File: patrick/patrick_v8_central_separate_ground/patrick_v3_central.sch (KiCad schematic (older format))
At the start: 32 parts, among them J1 Conn_02x05_Counter_Clockwise, J10 61300311121, J2 Conn_02x05_Counter_Clockwise, J3 Conn_02x05_Counter_Clockwise, J4 Conn_02x05_Counter_Clockwise, J5 Conn_02x05_Counter_Clockwise, J6 DM3CS-SF, J7 61300211121, J8 Conn_01x03, Q1 RUE002N02TL, Q2 RUE002N02TL, Q3 RUE002N02TL, U1 ICM-20948, U2 MCP1702T-1802E_CB, U3 BL652-SA-01, U4 PCA9685PW_Q900,118, U5 PCA9685PW_Q900,118, U6 MPM3610GQV-Z

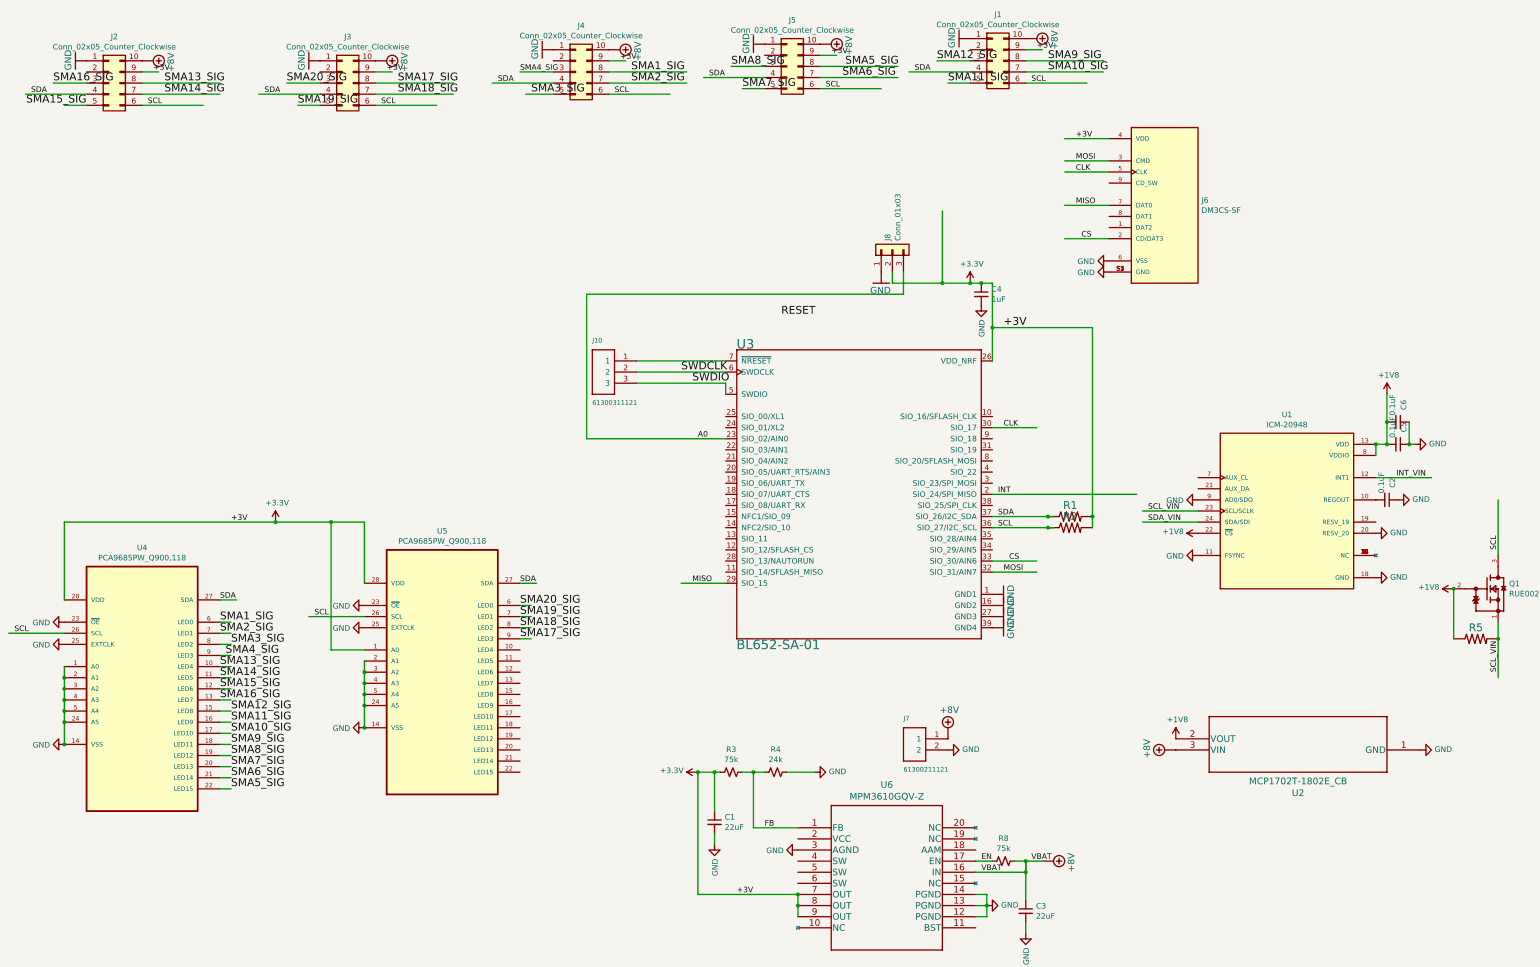
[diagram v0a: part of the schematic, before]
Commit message: separate gnd
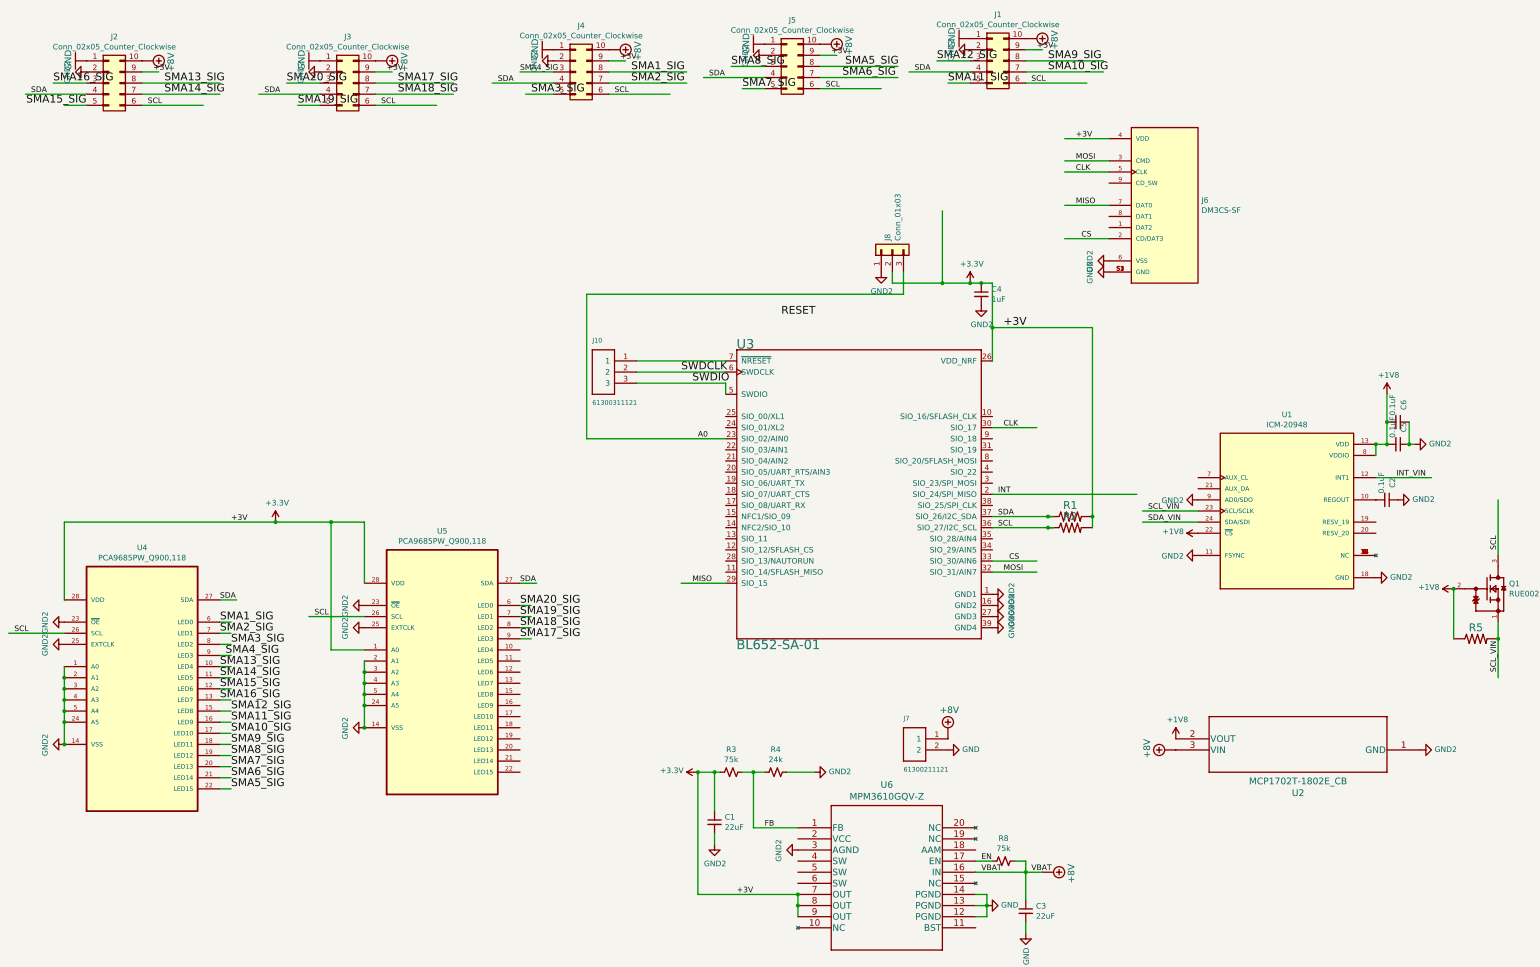
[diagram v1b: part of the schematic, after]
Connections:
- net labels added: GND2
- wire segments 157 -> 156

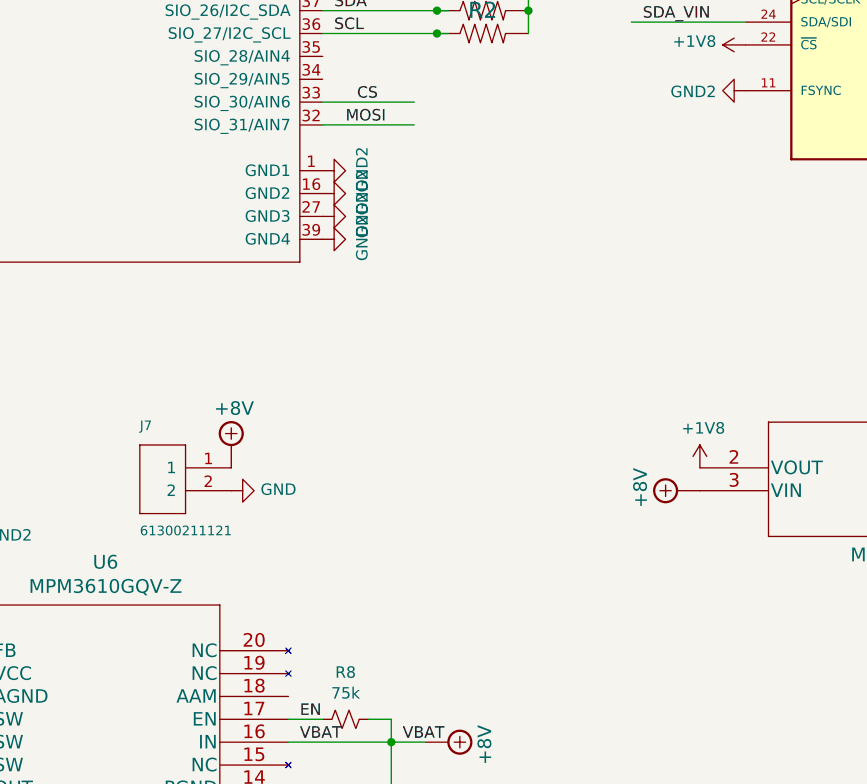
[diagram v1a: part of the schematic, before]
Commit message: separate gnd
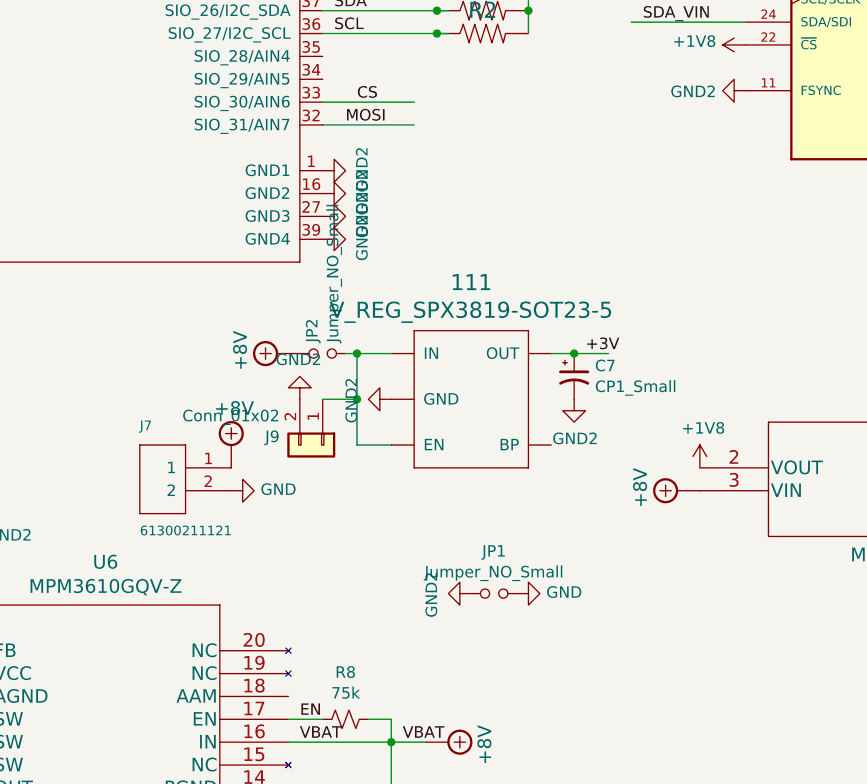
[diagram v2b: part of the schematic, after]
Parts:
- added 111: V_REG_SPX3819-SOT23-5, Package_TO_SOT_SMD:SOT-23-5, symbol patrick_0.5-eagle-import:V_REG_SPX3819-SOT23-5
- added C7: CP1_Small, Capacitor_THT:CP_Radial_D4.0mm_P2.00mm, symbol Device:CP1_Small
- added J9: Conn_01x02, Connector_PinSocket_2.00mm:PinSocket_1x02_P2.00mm_Vertical, symbol Connector_Generic:Conn_01x02
- added JP1, JP2: Jumper_NO_Small, Jumper:SolderJumper-2_P1.3mm_Open_RoundedPad1.0x1.5mm, symbol Device:Jumper_NO_Small
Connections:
- wire segments 156 -> 164
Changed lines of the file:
@@
 	0    -1   -1   0
 $EndComp
+$Comp
+L patrick_0.5-eagle-import:V_REG_SPX3819-SOT23-5 111
+U 1 1 62AABCB4
+P 9950 6800
+F 0 "111" H 9900 7310 70  0000 C CNN
+F 1 "V_REG_SPX3819-SOT23-5" H 9900 7189 70  0000 C CNN
+F 2 "Package_TO_SOT_SMD:SOT-23-5" H 9950 6800 50  0001 C CNN
+F 3 "" H 9950 6800 50  0001 C CNN
+	1    9950 6800
+	1    0    0    -1
+$EndComp
+$Comp
+L patrick_0.5-eagle-import:+8V #SUPPLY0107
+U 1 1 62ABC0BC
+P 9050 6600
+F 0 "#SUPPLY0107" H 9050 6600 50  0001 C CNN
+F 1 "+8V" H 8975 6725 59  0000 L BNN
+F 2 "" H 9050 6600 50  0001 C CNN
+F 3 "" H 9050 6600 50  0001 C CNN
+	1    9050 6600
+	0    -1   -1   0
+$EndComp
+Wire Wire Line
+	9400 6600 9550 6600
+Wire Wire Line
+	9400 6600 9400 6800
+Wire Wire Line
+	9400 7000 9550 7000
+Wire Wire Line
+	10250 6600 10350 6600
+Text Label 10400 6600 0    50   ~ 0
++3V
+$Comp
+L power:GND #PWR0142
+U 1 1 62AF45D3
+P 10100 7650
+F 0 "#PWR0142" H 10100 7400 50  0001 C CNN
+F 1 "GND" V 10105 7522 50  0000 R CNN
+F 2 "" H 10100 7650 50  0001 C CNN
+F 3 "" H 10100 7650 50  0001 C CNN
+	1    10100 7650
+	0    -1   -1   0
+$EndComp
+$Comp
+L power:GND2 #PWR0143
+U 1 1 62AF4B83
+P 9900 7650
+F 0 "#PWR0143" H 9900 7400 50  0001 C CNN
+F 1 "GND2" H 9905 7477 50  0000 C CNN
+F 2 "" H 9900 7650 50  0001 C CNN
+F 3 "" H 9900 7650 50  0001 C CNN
+	1    9900 7650
+	0    1    1    0
+$EndComp
+$Comp
+L Device:CP1_Small C7
+U 1 1 62AF58EE
+P 10350 6700
+F 0 "C7" H 10441 6746 50  0000 L CNN
+F 1 "CP1_Small" H 10441 6655 50  0000 L CNN
+F 2 "Capacitor_THT:CP_Radial_D4.0mm_P2.00mm" H 10350 6700 50  0001 C CNN
+F 3 "~" H 10350 6700 50  0001 C CNN
+	1    10350 6700
+	1    0    0    -1
+$EndComp
+Connection ~ 10350 6600
+Wire Wire Line
+	10350 6600 10500 6600
+$Comp
+L power:GND2 #PWR0144
+U 1 1 62AF7747
+P 10350 6800
+F 0 "#PWR0144" H 10350 6550 50  0001 C CNN
+F 1 "GND2" H 10355 6627 50  0000 C CNN
+F 2 "" H 10350 6800 50  0001 C CNN
+F 3 "" H 10350 6800 50  0001 C CNN
+	1    10350 6800
+	1    0    0    -1
+$EndComp
+$Comp
+L Device:Jumper_NO_Small JP1
+U 1 1 62AF8D43
+P 10000 7650
+F 0 "JP1" H 10000 7835 50  0000 C CNN
+F 1 "Jumper_NO_Small" H 10000 7744 50  0000 C CNN
+F 2 "Jumper:SolderJumper-2_P1.3mm_Open_RoundedPad1.0x1.5mm" H 10000 7650 50  0001 C CNN
+F 3 "~" H 10000 7650 50  0001 C CNN
+	1    10000 7650
+	1    0    0    -1
+$EndComp
+$Comp
+L Connector_Generic:Conn_01x02 J9
+U 1 1 62B24CAF
+P 9250 7000
+F 0 "J9" V 9214 6812 50  0000 R CNN
+F 1 "Conn_01x02" V 9123 6812 50  0000 R CNN
+F 2 "Connector_PinSocket_2.00mm:PinSocket_1x02_P2.00mm_Vertical" H 9250 7000 50  0001 C CNN
+F 3 "~" H 9250 7000 50  0001 C CNN
+	1    9250 7000
+	0    1    1    0
+$EndComp
+$Comp
+L Device:Jumper_NO_Small JP2
+U 1 1 62B2F037
+P 9250 6600
+F 0 "JP2" V 9204 6648 50  0000 L CNN
+F 1 "Jumper_NO_Small" V 9295 6648 50  0000 L CNN
+F 2 "Jumper:SolderJumper-2_P1.3mm_Open_RoundedPad1.0x1.5mm" H 9250 6600 50  0001 C CNN
+F 3 "~" H 9250 6600 50  0001 C CNN
+	1    9250 6600
+	1    0    0    -1
+$EndComp
+Wire Wire Line
+	9350 6600 9400 6600
+Connection ~ 9400 6600
+Wire Wire Line
+	9250 6800 9400 6800
+Connection ~ 9400 6800
+Wire Wire Line
+	9400 6800 9400 7000
+$Comp
+L power:GND2 #PWR0145
+U 1 1 62B25F72
+P 9150 6800
+F 0 "#PWR0145" H 9150 6550 50  0001 C CNN
+F 1 "GND2" H 9155 6627 50  0000 C CNN
+F 2 "" H 9150 6800 50  0001 C CNN
+F 3 "" H 9150 6800 50  0001 C CNN
+	1    9150 6800
+	-1   0    0    1
+$EndComp
+$Comp
+L power:GND2 #PWR0141
+U 1 1 62BEBDCF
+P 9550 6800
+F 0 "#PWR0141" H 9550 6550 50  0001 C CNN
+F 1 "GND2" H 9555 6627 50  0000 C CNN
+F 2 "" H 9550 6800 50  0001 C CNN
+F 3 "" H 9550 6800 50  0001 C CNN
+	1    9550 6800
+	0    1    1    0
+$EndComp
 $EndSCHEMATC
